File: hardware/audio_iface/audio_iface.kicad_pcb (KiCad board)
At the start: 2 copper layers, 70 x 66 mm, 83 parts, among them J201 UART, J301 LINEIN, J302 HP, J303 LINEOUT, J401 USB_C_Receptacle_USB2.0, U201 NUCLEO_L476RG, U301 SGTL5000XNAA3, U401 USBLC6-2SC6, U501 MCP23S17-E/SO

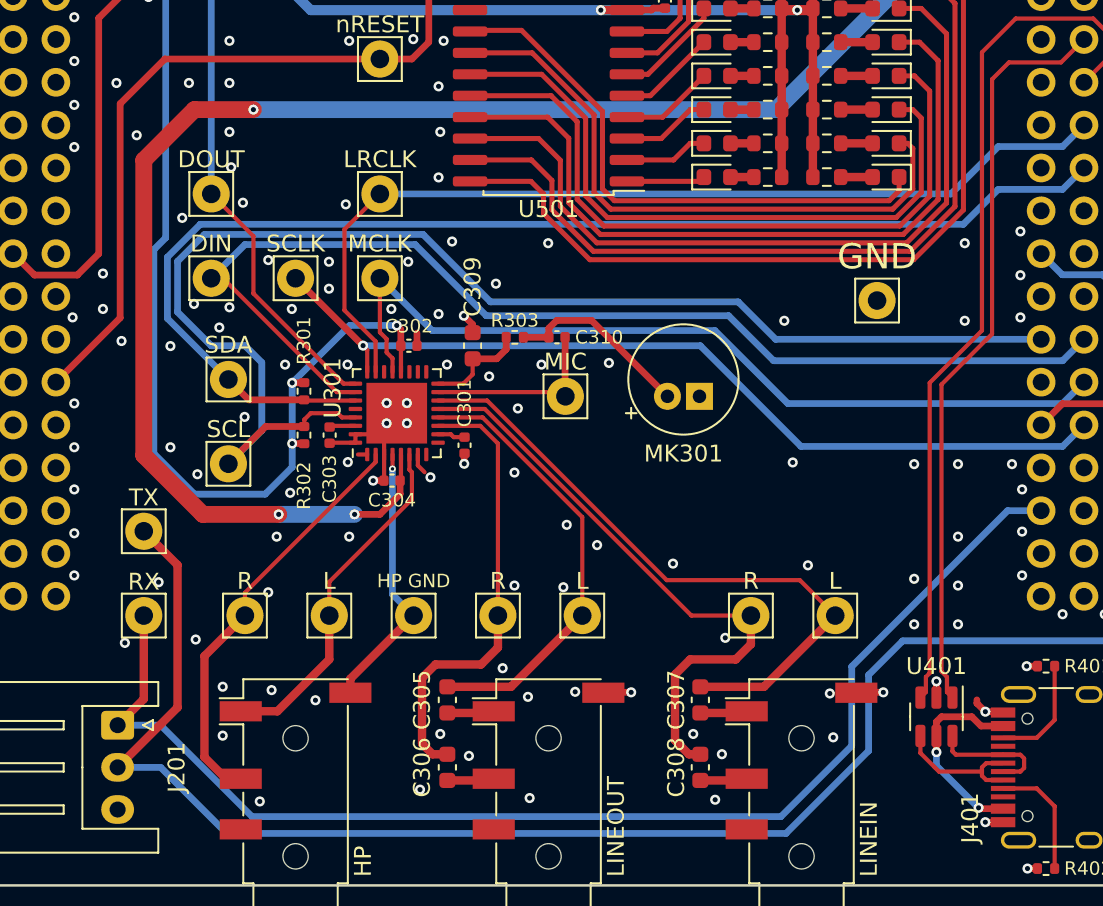
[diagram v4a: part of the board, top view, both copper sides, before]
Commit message: add logo
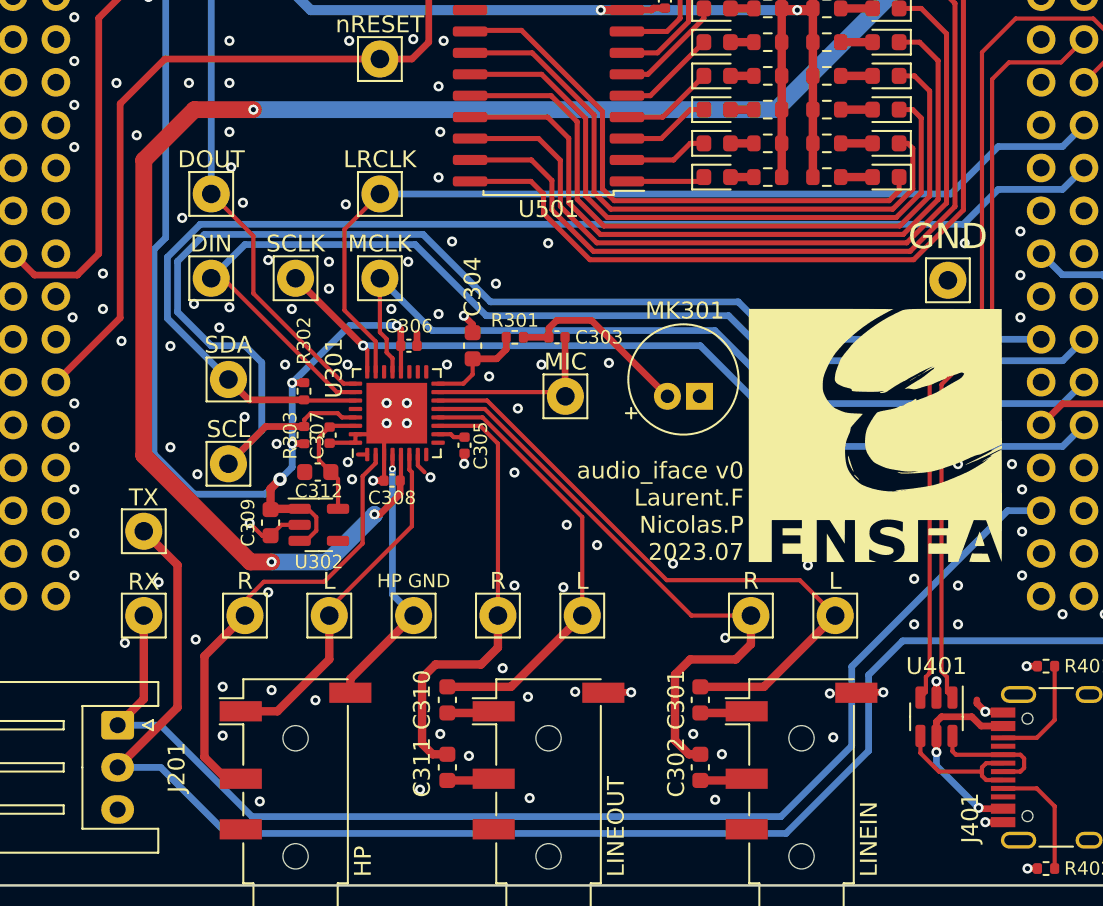
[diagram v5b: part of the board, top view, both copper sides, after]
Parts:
- added C309: 1u, Capacitor_SMD:C_0603_1608Metric, F.Cu at (33.5, 88.5)
- added C312: 1u, Capacitor_SMD:C_0603_1608Metric, F.Cu at (36.3, 85.5)
- added G***: LOGO, logo_ensea:logo_ensea_15mm, F.Cu at (69.4, 83.3)
- added U302: BU18SD2MG-MTR, Package_TO_SOT_SMD:SOT-23-5, F.Cu at (36.4, 88.6)
- moved TP205 4.37 mm to (73.7, 74.1)
- renumbered C307 to C301, C308 to C302, C310 to C303, C309 to C304, C301 to C305, C302 to C306, C303 to C307, C304 to C308, C305 to C310, C306 to C311, J303 to J302, J302 to J303, R303 to R301, R301 to R302, R302 to R303, TP108 to TP101, TP109 to TP102, TP110 to TP103, TP111 to TP104, TP112 to TP105, TP101 to TP106, TP102 to TP107, TP103 to TP108, TP104 to TP109, TP105 to TP110, TP106 to TP111, TP107 to TP112
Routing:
- net +3.3V: track 140.5 -> 146.6 mm, vias 6 -> 7
- net +1V8: track 1.56 -> 7.15 mm
- net GND: track 31.2 -> 34.7 mm
- net +3.3VA: track 99.1 -> 101.4 mm
- net /AUDIO CODEC/HP_R: track 24.8 -> 26.9 mm
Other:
- board text added: "audio_iface v0 Laurent.F Nicolas.P 2023.07"
